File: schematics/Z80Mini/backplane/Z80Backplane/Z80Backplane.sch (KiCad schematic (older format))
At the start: 11 parts, among them J1 Conn_02x20_Odd_Even, J2 Conn_02x20_Odd_Even, J3 Conn_02x20_Odd_Even, J4 Conn_02x20_Odd_Even, U1 L7805

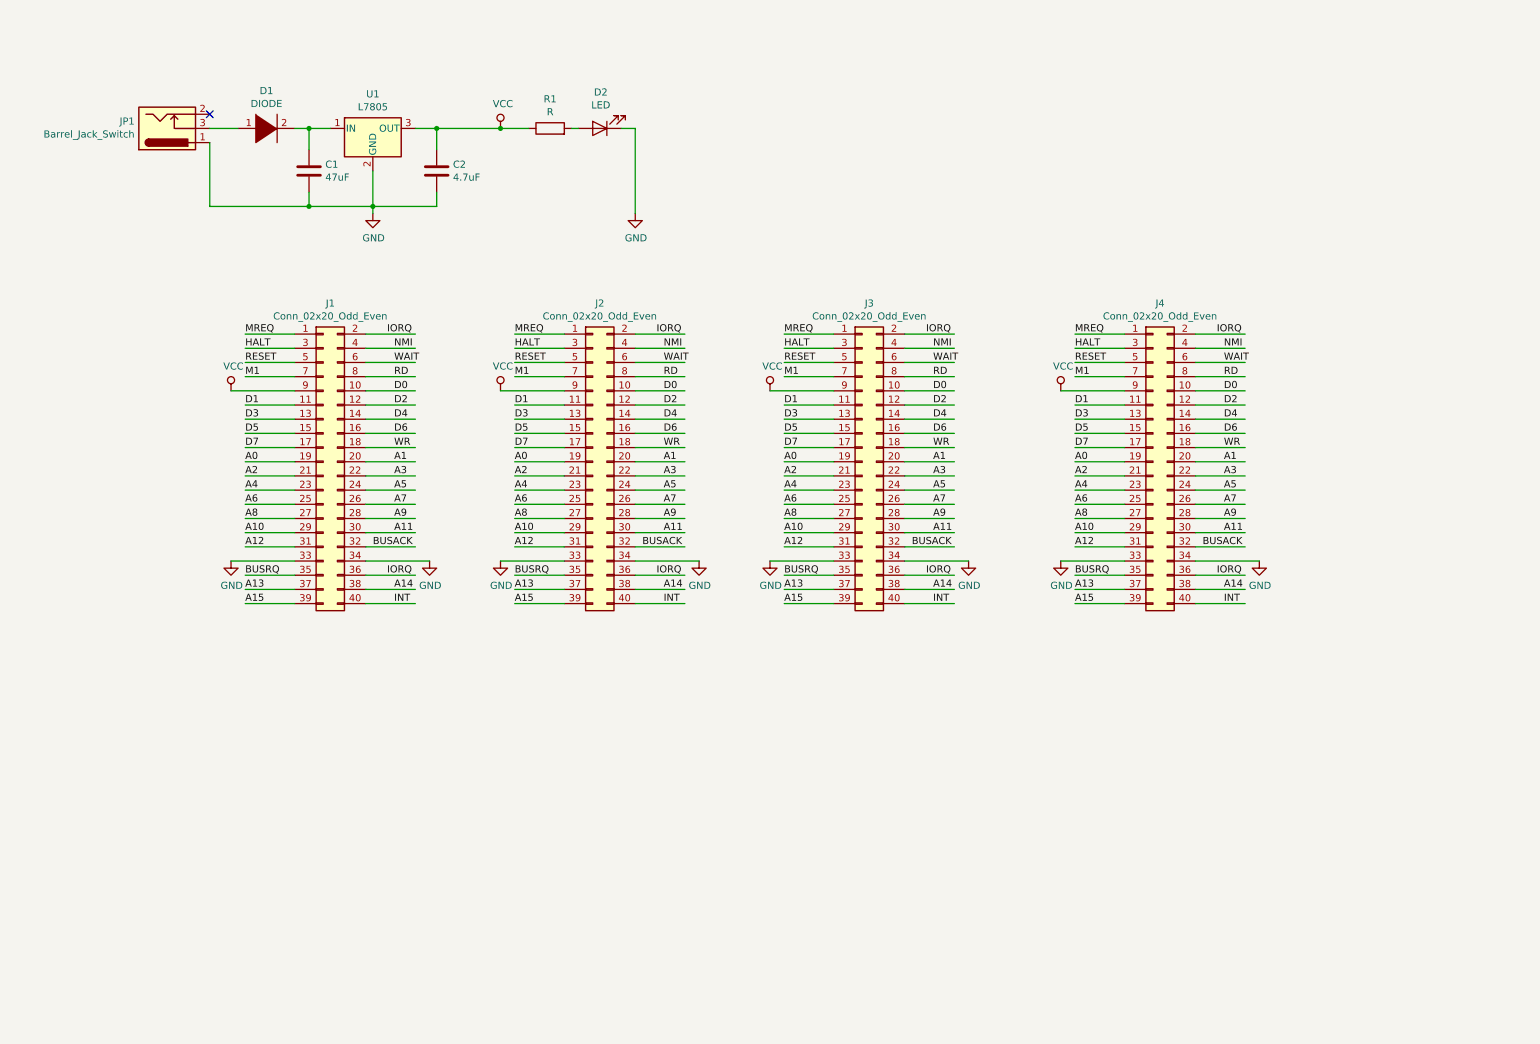
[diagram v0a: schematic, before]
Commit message: Testing C routines for VDP and keyboard. Generated backplane gerber files
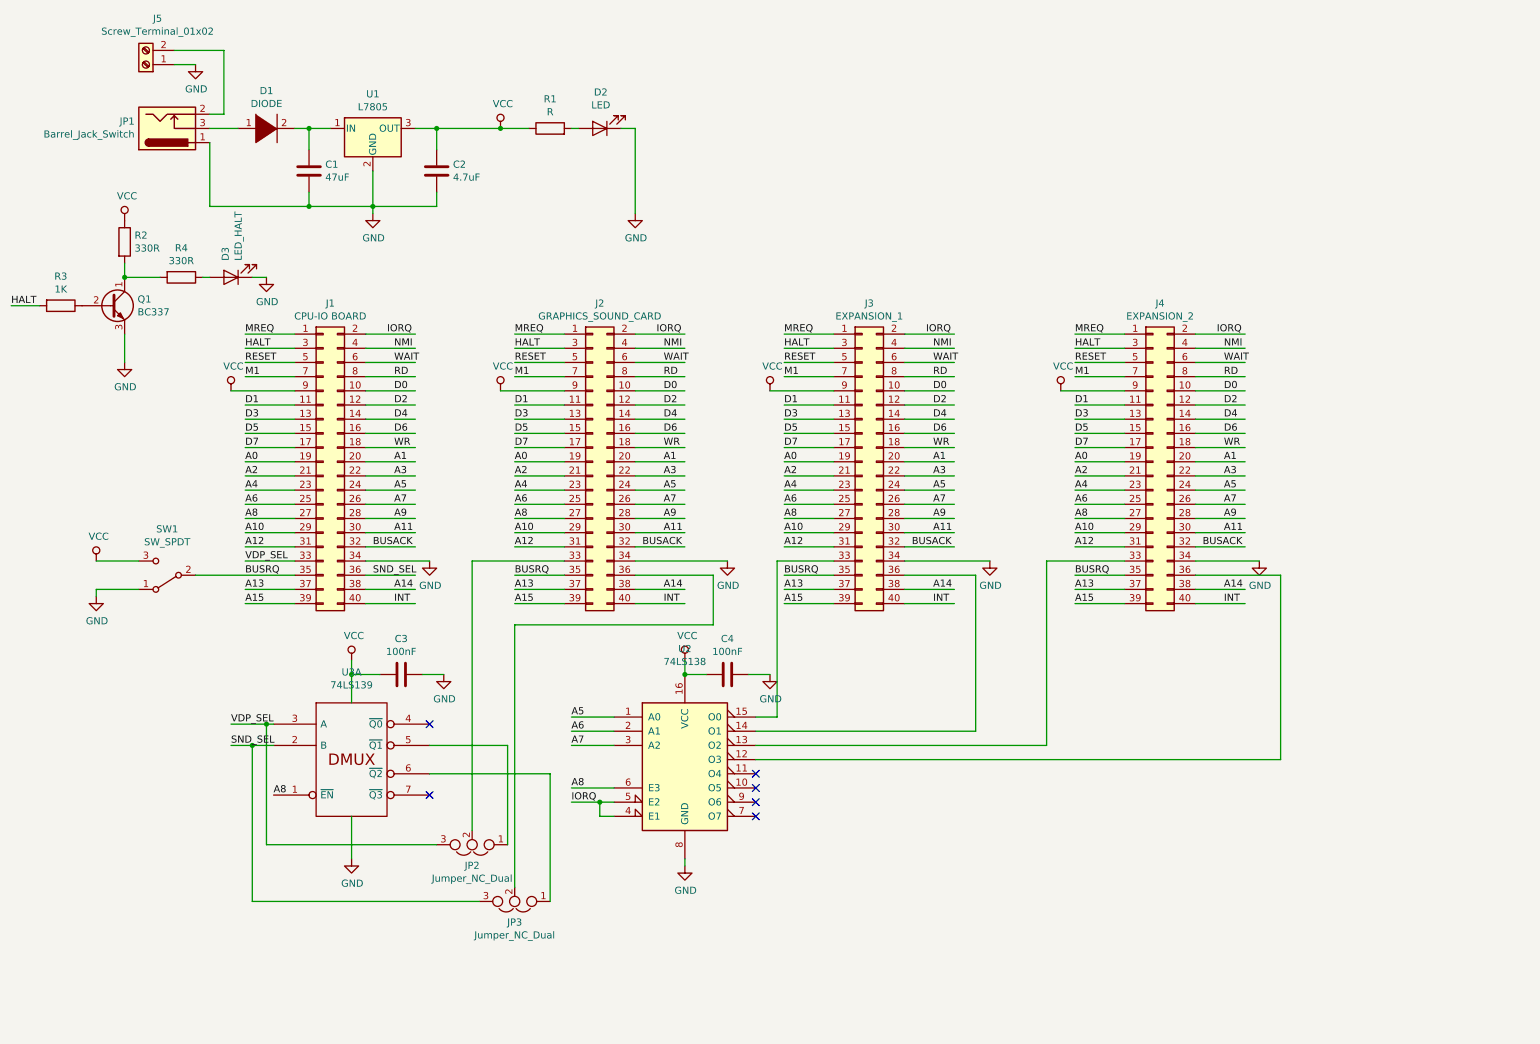
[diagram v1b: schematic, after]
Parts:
- added C3, C4: 100nF, Capacitor_THT:C_Disc_D7.0mm_W2.5mm_P5.00mm, symbol Device:C
- added D3: LED_HALT, LED_THT:LED_D3.0mm, symbol Device:LED
- added J5: Screw_Terminal_01x02, TerminalBlock:TerminalBlock_bornier-2_P5.08mm, symbol Connector:Screw_Terminal_01x02
- added JP2, JP3: Jumper_NC_Dual, Connector_PinHeader_2.54mm:PinHeader_1x03_P2.54mm_Vertical, symbol Device:Jumper_NC_Dual
- added Q1: BC337, Package_TO_SOT_THT:TO-92_Inline, symbol Transistor_BJT:BC337
- added R2, R4: 330R, Resistor_THT:R_Axial_DIN0207_L6.3mm_D2.5mm_P10.16mm_Horizontal, symbol Device:R
- added R3: 1K, Resistor_THT:R_Axial_DIN0207_L6.3mm_D2.5mm_P10.16mm_Horizontal, symbol Device:R
- added SW1: SW_SPDT, Connector_PinHeader_2.54mm:PinHeader_1x03_P2.54mm_Vertical, symbol Switch:SW_SPDT
- added U2: 74LS138, Package_DIP:DIP-16_W7.62mm_Socket, symbol 74xx:74LS138
- added U3: 74LS139, Package_DIP:DIP-16_W7.62mm_Socket, symbol 74xx_IEEE:74LS139
- C1, C2: footprint Capacitor_THT:C_Radial_D5.0mm_H11.0mm_P2.00mm -> Capacitor_THT:C_Radial_D6.3mm_H5.0mm_P2.50mm
- J1: value Conn_02x20_Odd_Even -> CPU-IO BOARD
- J2: value Conn_02x20_Odd_Even -> GRAPHICS_SOUND_CARD
- J3: value Conn_02x20_Odd_Even -> EXPANSION_1
- J4: value Conn_02x20_Odd_Even -> EXPANSION_2
- R1: footprint Resistor_THT:R_Axial_DIN0207_L6.3mm_D2.5mm_P7.62mm_Horizontal -> Resistor_THT:R_Axial_DIN0207_L6.3mm_D2.5mm_P10.16mm_Horizontal
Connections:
- net labels added: SND_SEL, VDP_SEL
- wire segments 179 -> 233
- no-connect marks 1 -> 6

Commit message: Latest code changes and modified Makefile to support burn to EPROM Emulator
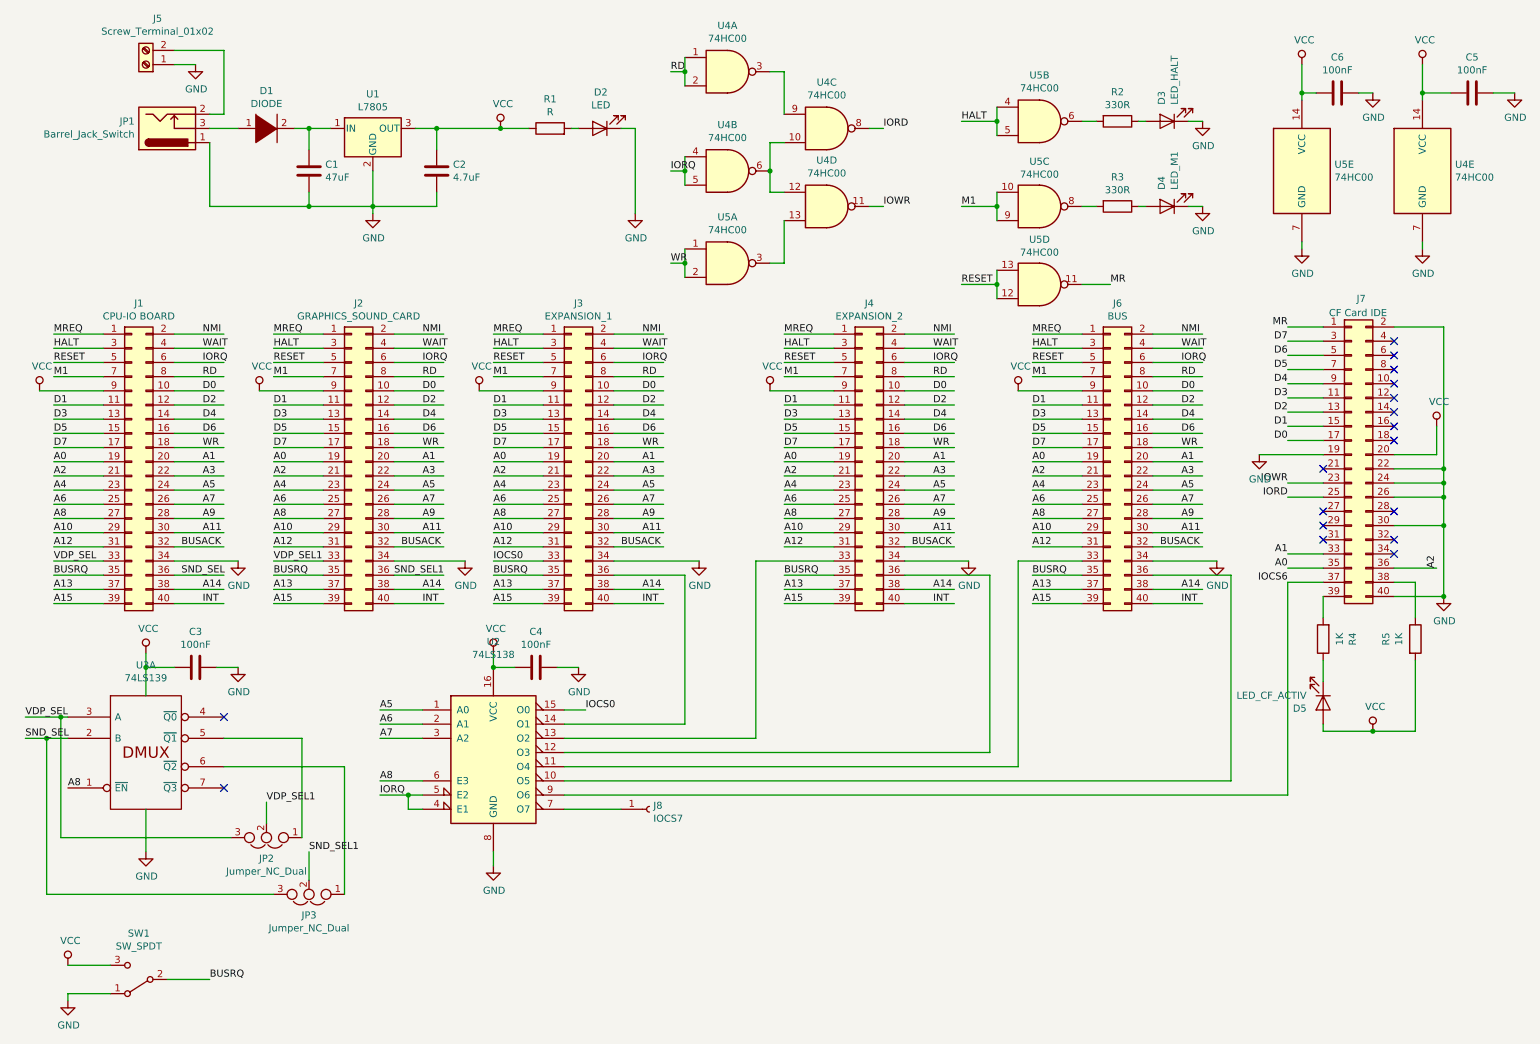
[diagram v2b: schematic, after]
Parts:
- removed Q1: BC337, Package_TO_SOT_THT:TO-92_Inline, symbol Transistor_BJT:BC337
- added C5, C6: 100nF, Capacitor_THT:C_Disc_D7.0mm_W2.5mm_P5.00mm, symbol Device:C
- added D4: LED_M1, LED_THT:LED_D3.0mm, symbol Device:LED
- added D5: LED_CF_ACTIV, LED_THT:LED_D3.0mm, symbol Device:LED
- added J6: BUS, Connector_IDC:IDC-Header_2x20_P2.54mm_Vertical, symbol Connector_Generic:Conn_02x20_Odd_Even
- added J7: CF Card IDE, Connector_PinHeader_2.00mm:PinHeader_2x20_P2.00mm_Vertical, symbol Connector_Generic:Conn_02x20_Odd_Even
- added J8: IOCS7, Connector_PinHeader_2.54mm:PinHeader_1x01_P2.54mm_Vertical, symbol Connector:Conn_01x01_Female
- added R5: 1K, Resistor_THT:R_Axial_DIN0207_L6.3mm_D2.5mm_P10.16mm_Horizontal, symbol Device:R
- added U4, U5: 74HC00, Package_DIP:DIP-14_W7.62mm, symbol 74xx:74HC00
- R3: value 1K -> 330R
- R4: value 330R -> 1K
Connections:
- net labels added: IOCS0, IOCS6, IORD, IOWR, MR, SND_SEL1, VDP_SEL1
- wire segments 233 -> 354
- no-connect marks 6 -> 17
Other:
- moved on the sheet: C3, C4, J1, J2, J3, J4, JP2, JP3, SW1, U2, U3A
